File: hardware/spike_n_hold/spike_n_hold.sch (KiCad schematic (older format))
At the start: 59 parts, among them J1 input_trigger_2, J2 input_trigger_1, J3 to_solenoid_2, J4 to_solenoid_1, J5 Conn_01x02, J6 Conn_01x02, Q1 MJH11021G, Q2 MJH11021G, Q3 MPSA42, Q4 MPSA42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

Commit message: Update board and add gerbers
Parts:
- added J7: Conn_01x02, Connector_JST:JST_XH_B2B-XH-A_1x02_P2.50mm_Vertical, symbol Connector_Generic:Conn_01x02
- C8: value 100nF -> 10nF
- R17: value 47 -> 330
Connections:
- net +24V: now also J7.1 (Pin_1)
- net GND: now also J7.2 (Pin_2)
- net at R15.2, U3.7 (DIS): now also R16.2; no longer R16.1
- net at C7.2, U3.2 (TR), U3.6 (THR): now also R16.1; no longer R16.2
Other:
- note added: "*"
- note added: "**"
- note added: "***"
- note added: "LM555's pin 3 frequency depends on pin 7 and 6 resistors values and\npin 2 capacitor value, provided pin 5 capacitor remains constant.\nThis configuration provides about 100kHz frequency. It can also be\nachieved with another set of components. The choice of components\ndepends solely on what is more convenient to use at the moment. This \nschematics takes into an account values of resistors and 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"
- moved on the sheet: C15, C7, C8, D17, H1, H2, H3, H4, J5, J6, L1, Q9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

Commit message: Make inductor's footprint unified across system
Now all inductors have the same footprint and component.
Some minor changes in silk layers: added values to resistors and arranged them in a more readable way
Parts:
- L1: footprint Inductor_THT:L_Radial_D7.5mm_P3.50mm_Fastron_07P -> Inductor_THT:L_Radial_D10.0mm_P5.00mm_Neosid_SD12_style3
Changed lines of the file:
@@
 F 0 "L1" V 9090 1450 50  0000 C CNN
 F 1 "33µH" V 8999 1450 50  0000 C CNN
-F 2 "Inductor_THT:L_Radial_D7.5mm_P3.50mm_Fastron_07P" H 8900 1450 50  0001 C CNN
+F 2 "Inductor_THT:L_Radial_D10.0mm_P5.00mm_Neosid_SD12_style3" H 8900 1450 50  0001 C CNN
 F 3 "~" H 8900 1450 50  0001 C CNN
 	1    8900 1450

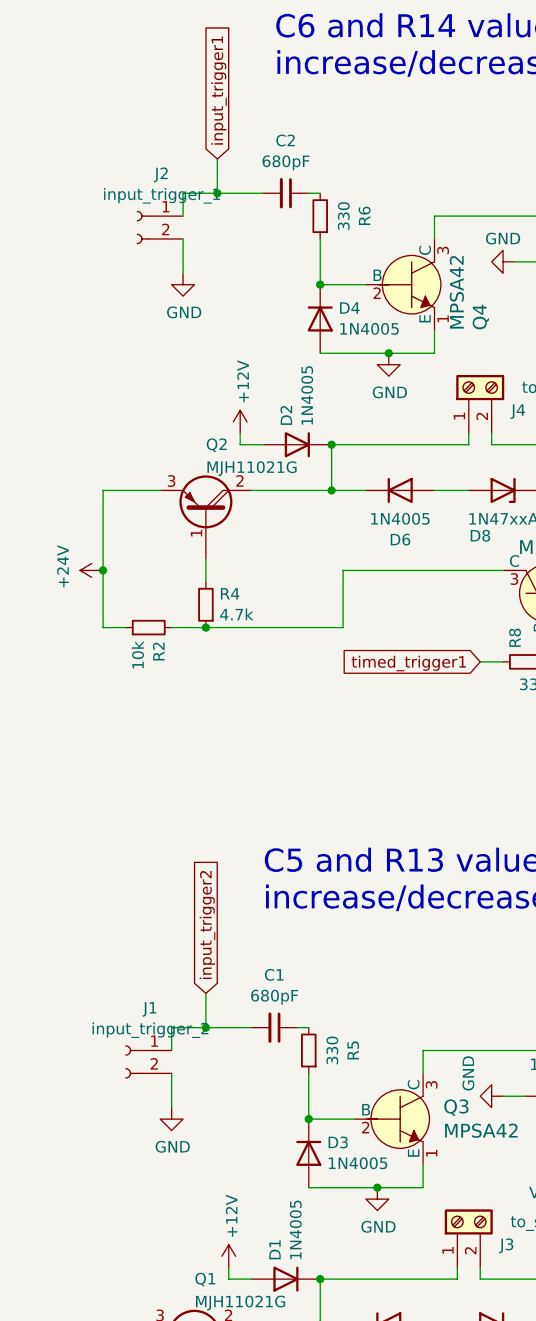
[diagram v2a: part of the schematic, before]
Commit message: update input pins, so that they are beehive compatible
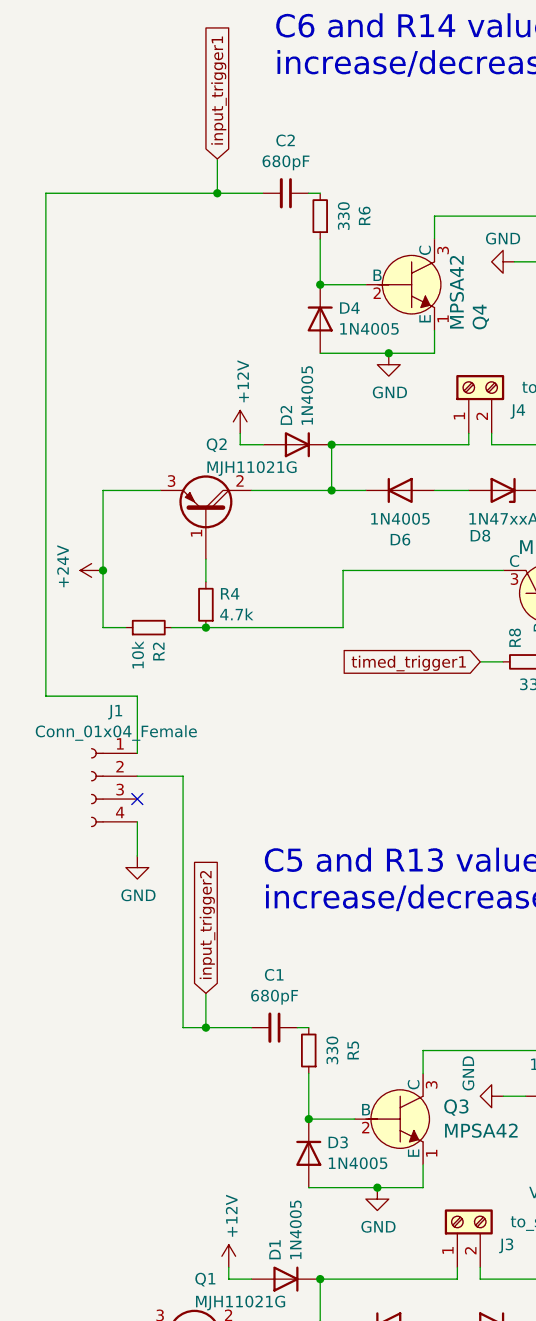
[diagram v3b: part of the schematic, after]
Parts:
- removed J1: input_trigger_2, Connector_PinHeader_2.54mm:PinHeader_1x02_P2.54mm_Vertical, symbol Connector:Conn_01x02_Female
- removed J2: input_trigger_1, Connector_PinHeader_2.54mm:PinHeader_1x02_P2.54mm_Vertical, symbol Connector:Conn_01x02_Female
- added J1: Conn_01x04_Female, Connector_JST:JST_XH_B4B-XH-A_1x04_P2.50mm_Vertical, symbol Connector:Conn_01x04_Female
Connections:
- net GND: now also J1.4 (Pin_4)
- net input_trigger1: now also J1.1 (Pin_1)
- net input_trigger2: now also J1.2 (Pin_2)
- no-connect marks 0 -> 1
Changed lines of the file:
@@
 $EndComp
-$Comp
-L power:GND #PWR03
-U 1 1 6055607C
-P 1100 5550
-F 0 "#PWR03" H 1100 5300 50  0001 C CNN
-F 1 "GND" H 1105 5377 50  0000 C CNN
-F 2 "" H 1100 5550 50  0001 C CNN
-F 3 "" H 1100 5550 50  0001 C CNN
-	1    1100 5550
-	1    0    0    -1
-$EndComp
-$Comp
-L Connector:Conn_01x02_Female J1
-U 1 1 60556076
-P 900 5300
-F 0 "J1" H 792 5485 50  0000 C CNN
-F 1 "input_trigger_2" H 792 5394 50  0000 C CNN
-F 2 "Connector_PinHeader_2.54mm:PinHeader_1x02_P2.54mm_Vertical" H 900 5300 50  0001 C CNN
-F 3 "~" H 900 5300 50  0001 C CNN
-	1    900  5300
-	-1   0    0    -1
-$EndComp
-Wire Wire Line
-	1100 5200 1100 5300
-Wire Wire Line
-	1100 5400 1100 5550
 $Comp
 L power:GND #PWR07
@@
 Text GLabel 1250 5050 1    50   Input ~ 0
 input_trigger2
-Wire Wire Line
-	1100 5200 1250 5200
 Wire Wire Line
 	1250 5050 1250 5200
@@
 $EndComp
 $Comp
-L power:GND #PWR04
-U 1 1 6038634E
-P 1150 1900
-F 0 "#PWR04" H 1150 1650 50  0001 C CNN
-F 1 "GND" H 1155 1727 50  0000 C CNN
-F 2 "" H 1150 1900 50  0001 C CNN
-F 3 "" H 1150 1900 50  0001 C CNN
-	1    1150 1900
-	1    0    0    -1
-$EndComp
-$Comp
-L Connector:Conn_01x02_Female J2
-U 1 1 60386348
-P 950 1650
-F 0 "J2" H 842 1835 50  0000 C CNN
-F 1 "input_trigger_1" H 842 1744 50  0000 C CNN
-F 2 "Connector_PinHeader_2.54mm:PinHeader_1x02_P2.54mm_Vertical" H 950 1650 50  0001 C CNN
-F 3 "~" H 950 1650 50  0001 C CNN
-	1    950  1650
-	-1   0    0    -1
-$EndComp
-Wire Wire Line
-	1150 1550 1150 1650
-Wire Wire Line
-	1150 1750 1150 1900
-$Comp
 L power:GND #PWR08
 U 1 1 60386340
@@
 Text GLabel 1300 1400 1    50   Input ~ 0
 input_trigger1
-Wire Wire Line
-	1150 1550 1300 1550
 Wire Wire Line
 	1300 1400 1300 1550
@@
 Text Notes 8700 2550 0    50   ~ 0
 **
+$Comp
+L Connector:Conn_01x04_Female J1
+U 1 1 60DA480F
+P 750 4100
+F 0 "J1" H 642 4385 50  0000 C CNN
+F 1 "Conn_01x04_Female" H 642 4294 50  0000 C CNN
+F 2 "Connector_JST:JST_XH_B4B-XH-A_1x04_P2.50mm_Vertical" H 750 4100 50  0001 C CNN
+F 3 "~" H 750 4100 50  0001 C CNN
+	1    750  4100
+	-1   0    0    -1
+$EndComp
+Wire Wire Line
+	950  4100 1150 4100
+Wire Wire Line
+	1150 4100 1150 5200
+Wire Wire Line
+	1150 5200 1250 5200
+Wire Wire Line
+	950  4000 950  3750
+Wire Wire Line
+	950  3750 550  3750
+Wire Wire Line
+	550  3750 550  1550
+Wire Wire Line
+	550  1550 1300 1550
+NoConn ~ 950  4200
+$Comp
+L power:GND #PWR03
+U 1 1 60DF0A92
+P 950 4450
+F 0 "#PWR03" H 950 4200 50  0001 C CNN
+F 1 "GND" H 955 4277 50  0000 C CNN
+F 2 "" H 950 4450 50  0001 C CNN
+F 3 "" H 950 4450 50  0001 C CNN
+	1    950  4450
+	1    0    0    -1
+$EndComp
+Wire Wire Line
+	950  4300 950  4450
 $EndSCHEMATC
